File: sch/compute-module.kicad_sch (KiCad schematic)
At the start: 9 parts, among them J2 SAM10346-ND, J3 Conn_02x20_Odd_Even, M1 ComputeModule5-CM5, SW1 1825910-6

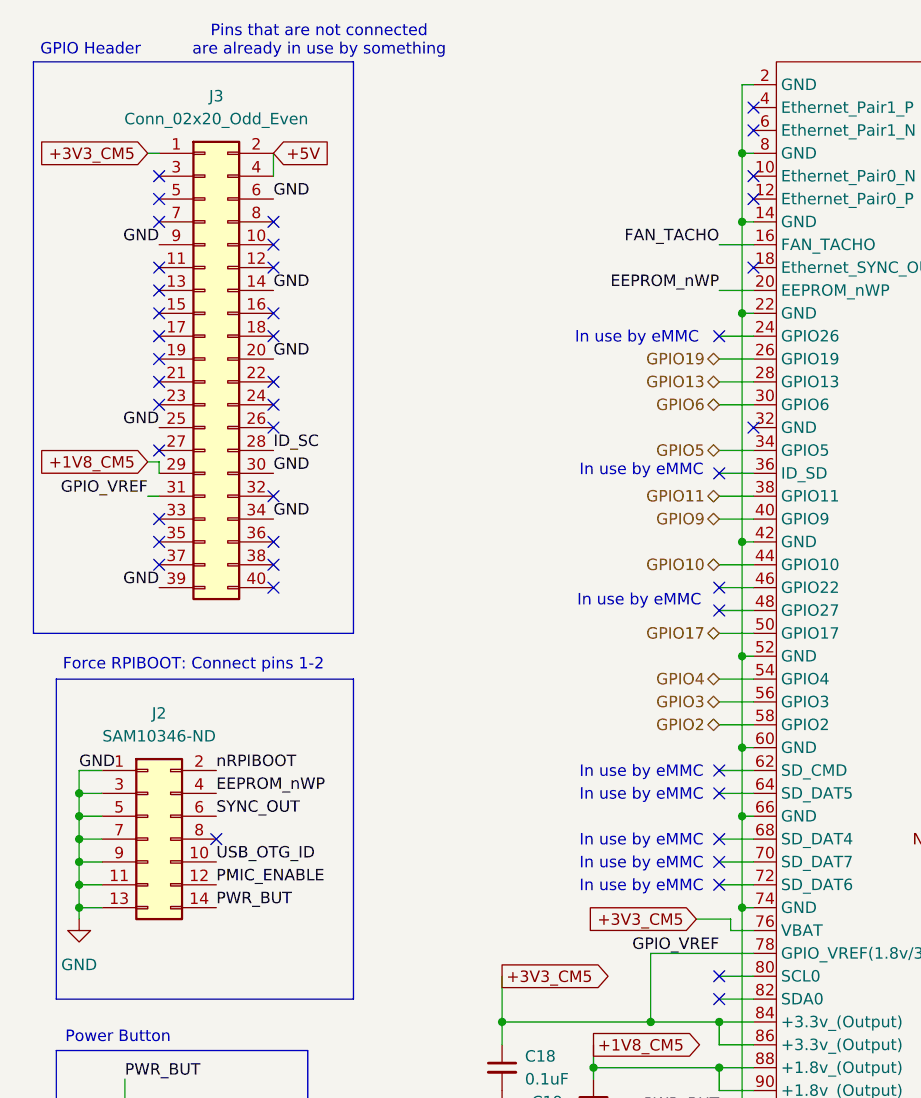
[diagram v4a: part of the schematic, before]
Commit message: Added new GPIO header, 7x2 vs 10x2, gonnected GPIO's and CM power to header
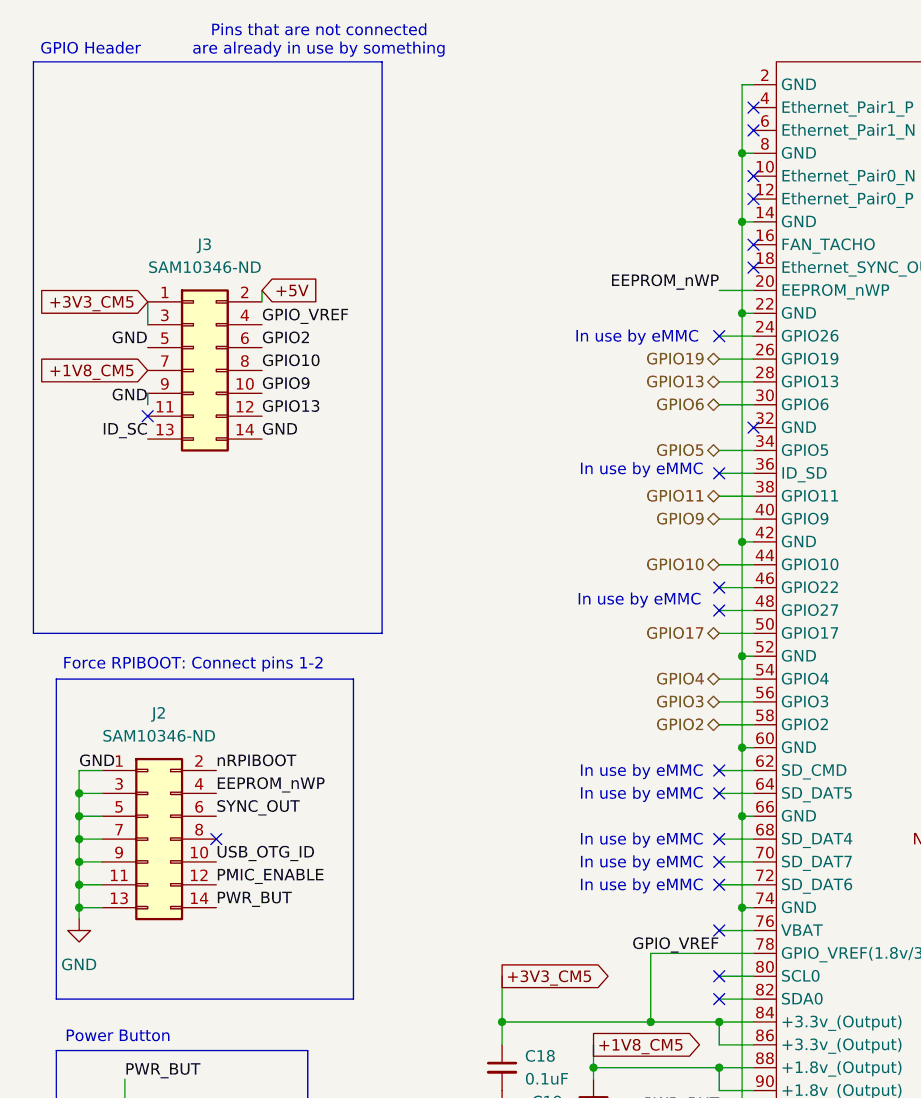
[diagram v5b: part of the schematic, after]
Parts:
- removed J3: Conn_02x20_Odd_Even, Connector_PinSocket_2.54mm:PinSocket_2x20_P2.54mm_Vertical, symbol Connector_Generic:Conn_02x20_Odd_Even
- added J3: SAM10346-ND, Connector_PinSocket_2.54mm:PinSocket_2x07_P2.54mm_Vertical, symbol Connector_Generic:Conn_02x07_Odd_Even
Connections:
- net +1V8_CM5: now also J3.7 (Pin_7)
- net +3V3_CM5: now also J3.1 (Pin_1), J3.3 (Pin_3), J3.4 (Pin_4); no longer M1.76 (VBAT)
- net +5V: now also J3.2 (Pin_2)
- net GND: now also J3.14 (Pin_14), J3.5 (Pin_5), J3.9 (Pin_9)
- net GPIO10: now also J3.8 (Pin_8)
- net GPIO13: now also J3.12 (Pin_12)
- net GPIO2: now also J3.6 (Pin_6)
- net GPIO9: now also J3.10 (Pin_10)
- net ID_SC: now also J3.13 (Pin_13)
- net FAN_TACHO: no longer names the net of M1.16 (FAN_TACHO)
- no-connect marks 109 -> 86

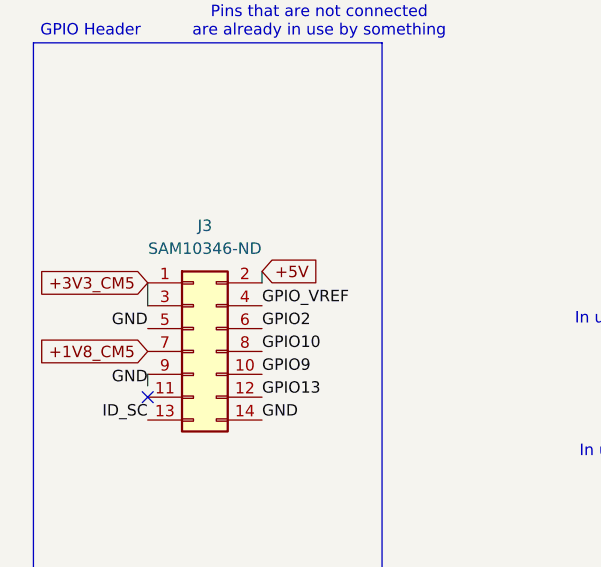
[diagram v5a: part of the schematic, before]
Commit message: added libs for footprints
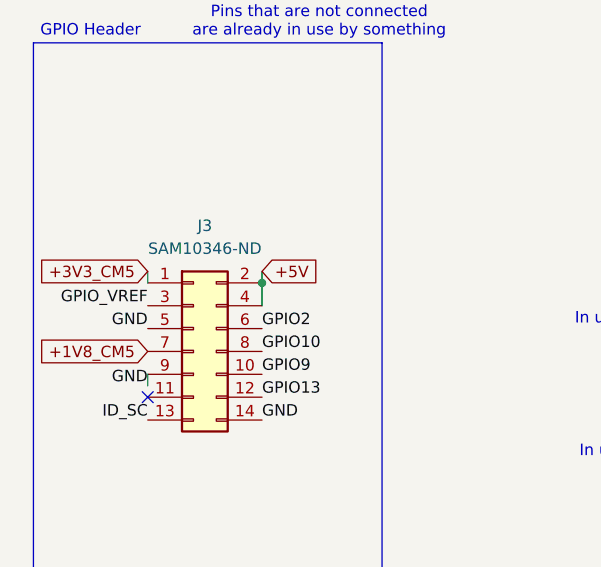
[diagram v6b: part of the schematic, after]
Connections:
- net +3V3_CM5: no longer J3.4 (Pin_4)
- net +5V: now also J3.4 (Pin_4)
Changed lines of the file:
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@@
+	)
+	(junction
+		(at 41.91 49.53)
+		(diameter 0)
+		(color 0 0 0 0)
 	)
 	(junction
@@
 	(wire
 		(pts
+			(xy 41.91 49.53) (xy 41.91 52.07)
+		)
+		(stroke
+			(width 0)
+			(type default)
+		)
+	)
+	(wire
+		(pts
 			(xy 92.71 129.54) (xy 92.71 132.08)
 		)
@@
 	(wire
 		(pts
-			(xy 29.21 49.53) (xy 29.21 52.07)
-		)
-		(stroke
-			(width 0)
-			(type default)
-		)
-	)
-	(wire
-		(pts
 			(xy 157.48 121.92) (xy 161.29 121.92)
 		)
@@
 		(pts
 			(xy 265.43 27.94) (xy 261.62 27.94)
+		)
+		(stroke
+			(width 0)
+			(type default)
+		)
+	)
+	(wire
+		(pts
+			(xy 29.21 48.26) (xy 29.21 49.53)
 		)
 		(stroke
@@
 	)
 	(label "GPIO_VREF"
-		(at 41.91 52.07 0)
-		(effects
-			(font
-				(size 1.27 1.27)
-			)
-			(justify left bottom)
+		(at 29.21 52.07 180)
+		(effects
+			(font
+				(size 1.27 1.27)
+			)
+			(justify right bottom)
 		)
 	)
@@
 	(global_label "+3V3_CM5"
 		(shape input)
-		(at 29.21 49.53 180)
+		(at 29.21 48.26 180)
 		(fields_autoplaced yes)
 		(effects
@@
 		)
 		(property "Intersheetrefs" "${INTERSHEET_REFS}"
-			(at 16.2463 49.53 0)
+			(at 16.2463 48.26 0)
 			(effects
 				(font
